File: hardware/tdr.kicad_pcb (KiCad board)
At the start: 4 copper layers, 232 parts, among them J201 Conn_02x01, J202 Conn_Coaxial, J203 Conn_Coaxial, J204 Conn_Coaxial, J205 Conn_Coaxial, J206 Conn_Coaxial, J207 Conn_Coaxial, J208 Conn_Coaxial, J209 Conn_Coaxial, J210 Barrel_Jack_Switch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

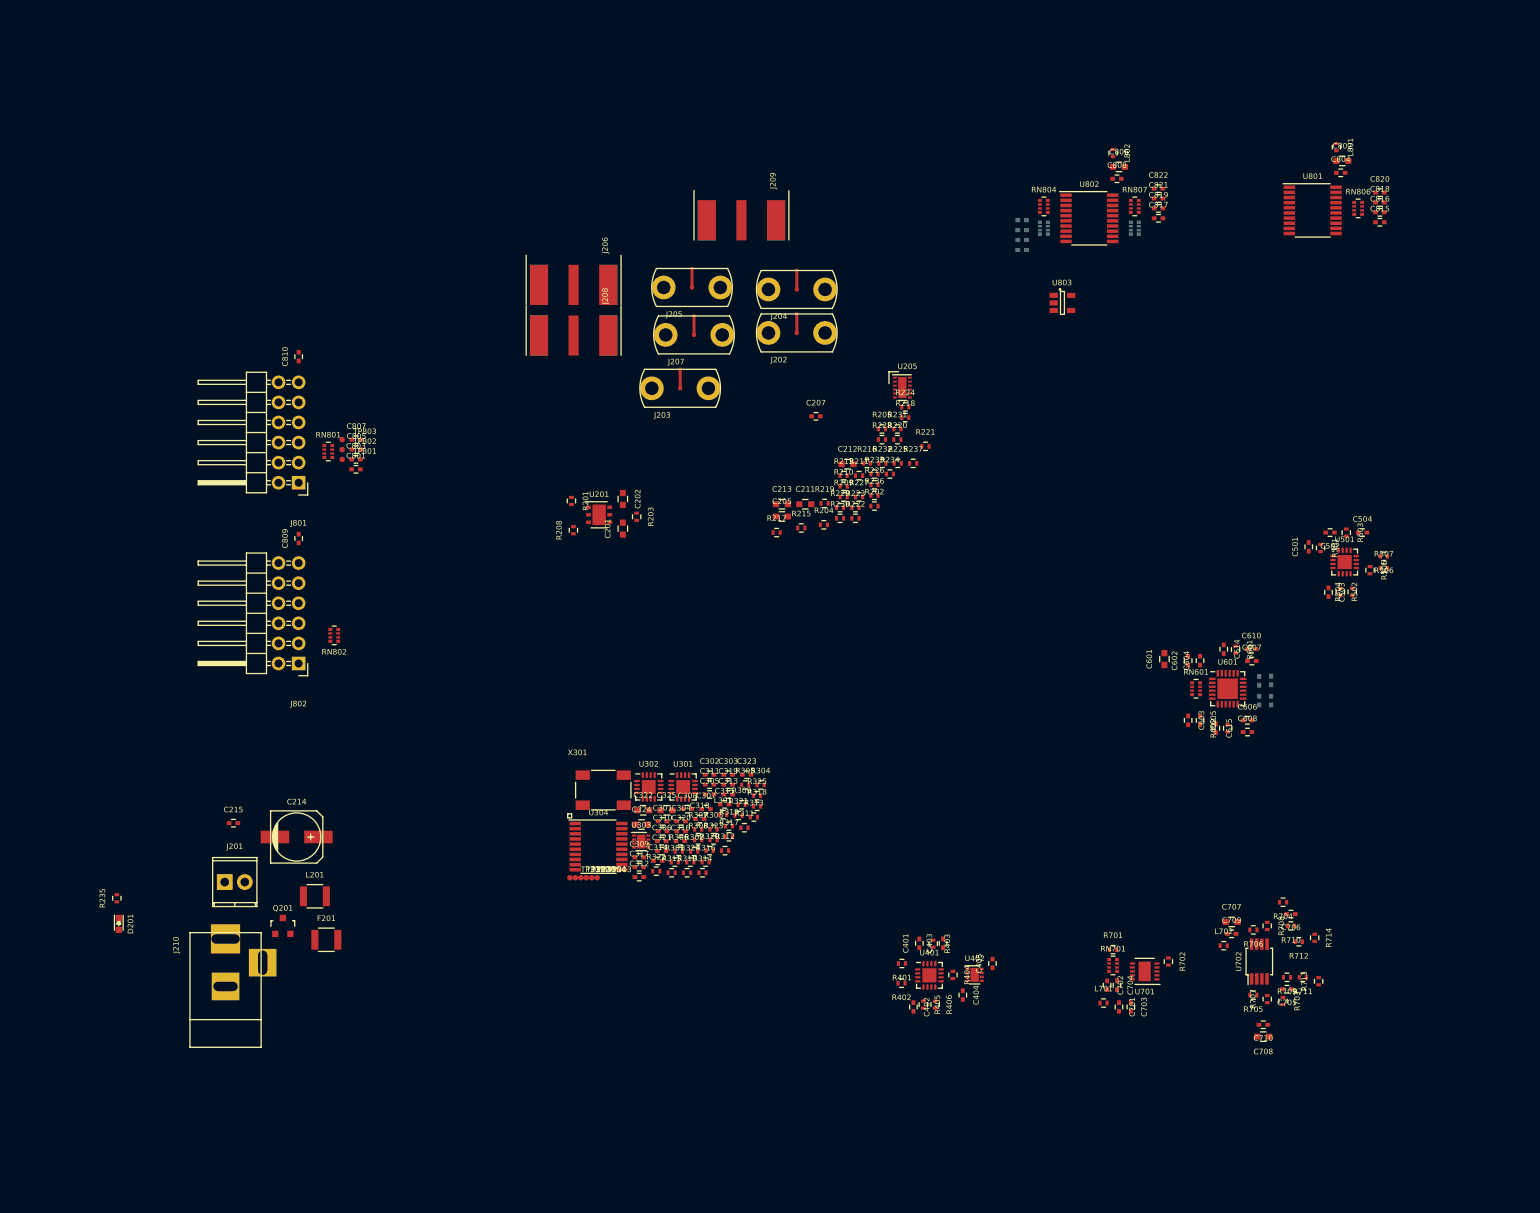
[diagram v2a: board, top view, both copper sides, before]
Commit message: more component placement on tdr..
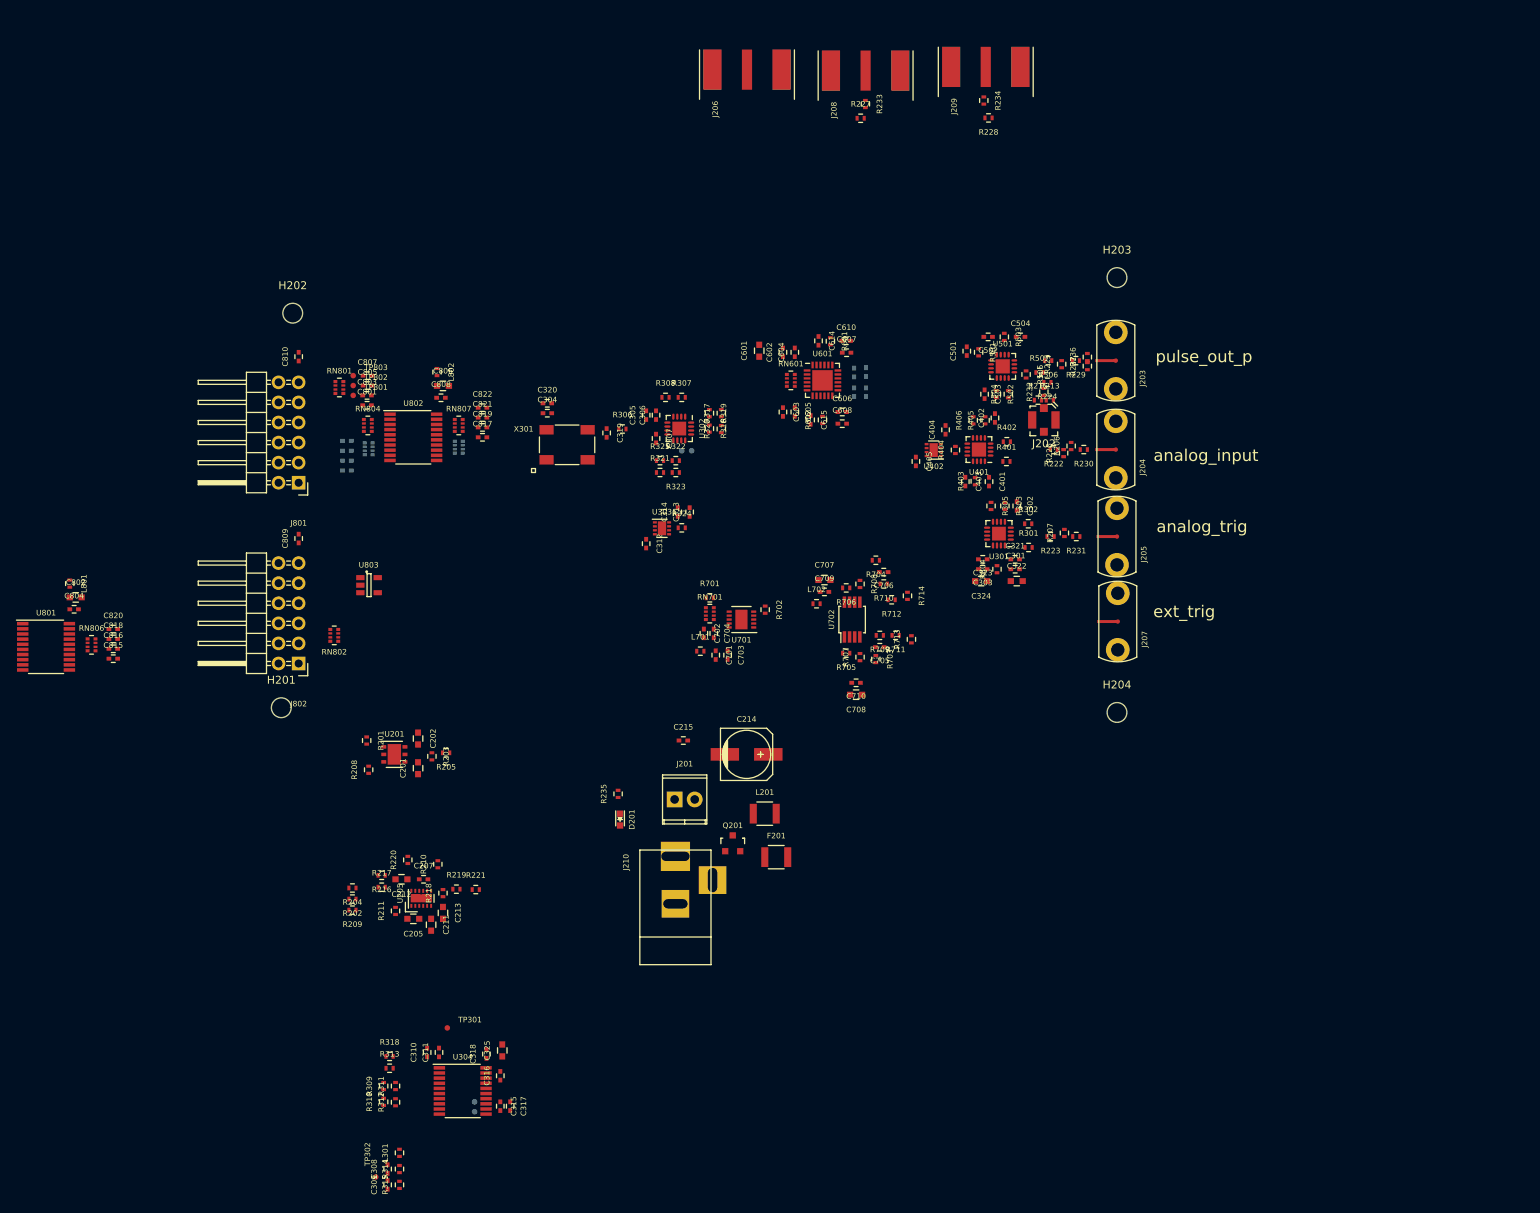
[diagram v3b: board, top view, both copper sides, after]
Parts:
- added H201: MountingHole, Mounting_Holes:MountingHole_2-5mm, F.Cu at (92.8, 104.4)
- added H202: MountingHole, Mounting_Holes:MountingHole_2-5mm, F.Cu at (94.2, 54.5)
- added H203: MountingHole, Mounting_Holes:MountingHole_2-5mm, F.Cu at (198.5, 50.0)
- added H204: MountingHole, Mounting_Holes:MountingHole_2-5mm, F.Cu at (198.5, 105.0)
- added R206: DNP, Resistors_SMD:R_0402, F.Cu at (192.7, 71.3)
- added R207: DNP, Resistors_SMD:R_0402, F.Cu at (191.8, 82.3)
- J202: footprint vna_footprints:SF2921-61345 -> vna_footprints:734120110_ufl_umc
- TP303, TP304, TP305, TP306: moved to B.Cu
- moved C804 169.4 mm to (66.6, 92.0)
- moved C802 169.4 mm to (66.8, 90.5)
- moved C815 169.4 mm to (71.5, 98.2)
- moved C816 169.4 mm to (71.5, 97.0)
- moved C818 169.4 mm to (71.5, 95.7)
- moved C820 169.4 mm to (71.5, 94.5)
- moved L801 169.4 mm to (66.0, 88.7)
- moved RN806 169.4 mm to (68.8, 96.5)
- moved U801 169.4 mm to (63.0, 96.7)
- moved U803 94.7 mm to (103.9, 88.9)
- moved C806 89.9 mm to (113.2, 63.7)
- moved C808 89.9 mm to (113.0, 65.2)
- moved C817 89.9 mm to (118.2, 70.2)
- moved C819 89.9 mm to (118.2, 69.0)
- moved C821 89.9 mm to (118.2, 67.7)
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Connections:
- R222 pad 1: Net-(R222-Pad1) -> Net-(R206-Pad1)
- R223 pad 1: Net-(R223-Pad1) -> Net-(R207-Pad1)
- R225 pad 1: Net-(R222-Pad1) -> Net-(R206-Pad2)
- R226 pad 1: Net-(R223-Pad1) -> Net-(R207-Pad2)
- R226 pad 2: Net-(R222-Pad1) -> Net-(R206-Pad1)
- R230 pad 2: Net-(R222-Pad1) -> Net-(R206-Pad1)
- R231 pad 2: Net-(R223-Pad1) -> Net-(R207-Pad1)
- R236 pad 2: (no net) -> GND
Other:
- board text added: "analog_input"
- board text added: "analog_trig"
- board text added: "ext_trig"
- board text added: "pulse_out_p"

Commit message: added rf crossover for latch trigger line to help with layout
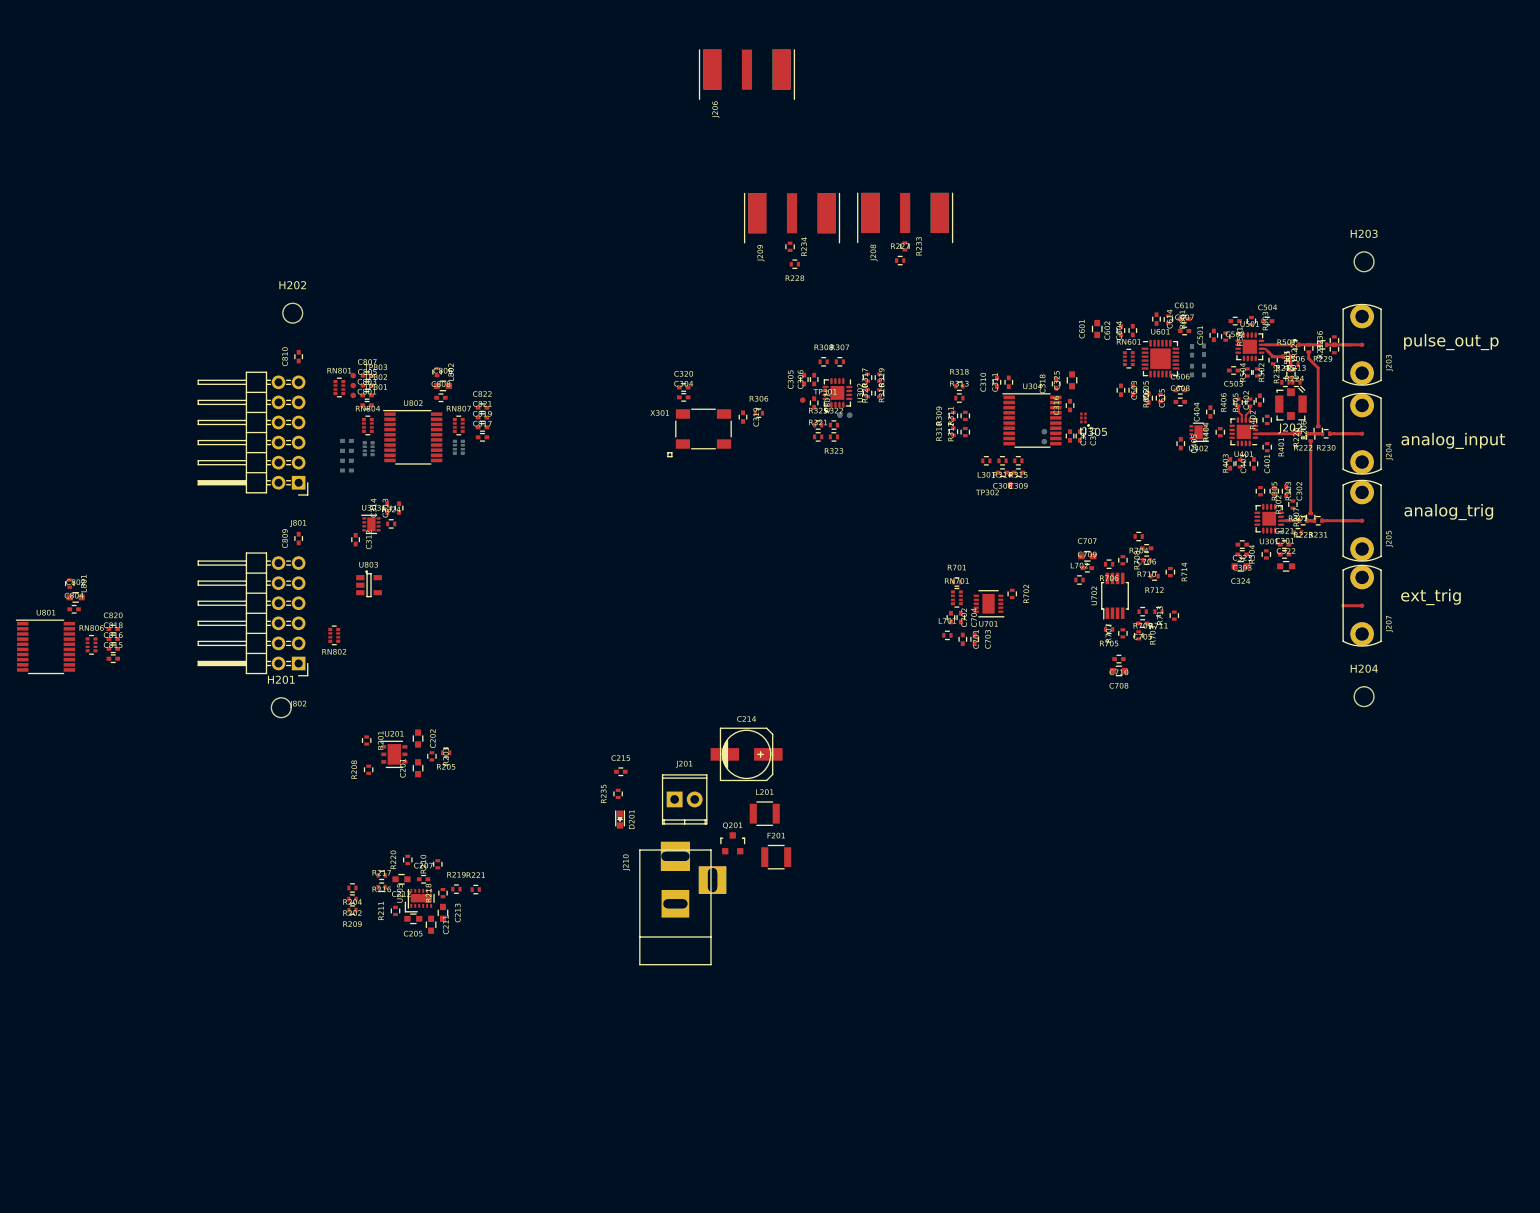
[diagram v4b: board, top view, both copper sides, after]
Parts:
- added U305: X0060L5050AHF, synth_footprints:X0060L5050AHF, F.Cu at (194.2, 67.8)
- moved R315 120.5 mm to (186.0, 73.2), turned to 180 degrees
- moved C309 120.3 mm to (186.0, 74.7), turned to 180 degrees
- moved TP302 118.8 mm to (185.0, 76.2), turned to 180 degrees
- moved R314 117.7 mm to (184.0, 73.2), turned to 180 degrees
- moved C308 117.5 mm to (184.0, 74.7), turned to 180 degrees
- moved L301 114.8 mm to (182.0, 73.2), turned to 180 degrees
- moved U304 111.3 mm to (187.8, 68.1)
- moved C310 111.3 mm to (183.3, 63.2)
- moved C311 111.3 mm to (184.8, 63.2)
- moved C315 111.3 mm to (192.6, 70.0)
- moved C317 111.3 mm to (193.8, 70.0)
- moved C325 111.3 mm to (192.8, 63.0)
- moved R309 111.3 mm to (177.8, 67.5)
- moved R310 111.3 mm to (177.8, 69.5)
- moved R311 111.3 mm to (179.3, 67.5)
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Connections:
- R405 pad 2: /delay_pulse/~DELAY1_OUT -> /~LATCH
- R406 pad 2: /delay_pulse/DELAY1_OUT -> /LATCH
- U304 pad 15: /CLK_SAMPLE_N -> Net-(U304-Pad15)
- U304 pad 16: /CLK_SAMPLE_P -> Net-(U304-Pad16)
- U601 pad 13: /delay_pulse/~DELAY1_OUT -> /LATCH
- U601 pad 14: /delay_pulse/DELAY1_OUT -> /~LATCH
- U601 pad 8: /CLK_SAMPLE_P -> /CLK_SAMPLE_N
- U601 pad 9: /CLK_SAMPLE_N -> /CLK_SAMPLE_P
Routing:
- net Net-(R206-Pad2): track 0.00 -> 9.95 mm
- net Net-(R207-Pad2): track 0.00 -> 9.20 mm
- net /conn_power/ANALOG_INPUT: track 0.00 -> 5.59 mm
- net Net-(J205-Pad1): track 0.00 -> 4.05 mm
- net Net-(R506-Pad2): track 0.00 -> 3.83 mm
- net Net-(J203-Pad1): track 0.00 -> 3.30 mm
- net Net-(R505-Pad1): track 0.00 -> 3.14 mm
- net Net-(J204-Pad1): track 0.00 -> 2.90 mm
- net /conn_power/PULSE_OUT_P: track 0.00 -> 2.60 mm
- net /EXT_ANALOG_TRIG: track 0.00 -> 2.59 mm
- net Net-(R206-Pad1): track 0.00 -> 2.00 mm
- net Net-(R405-Pad1): track 0.00 -> 1.99 mm
- net Net-(R406-Pad1): track 0.00 -> 1.97 mm
- net /conn_power/PULSE_OUT_N: track 0.00 -> 1.04 mm
- net Net-(R207-Pad1): track 0.00 -> 1.00 mm

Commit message: more component placement on tdr..
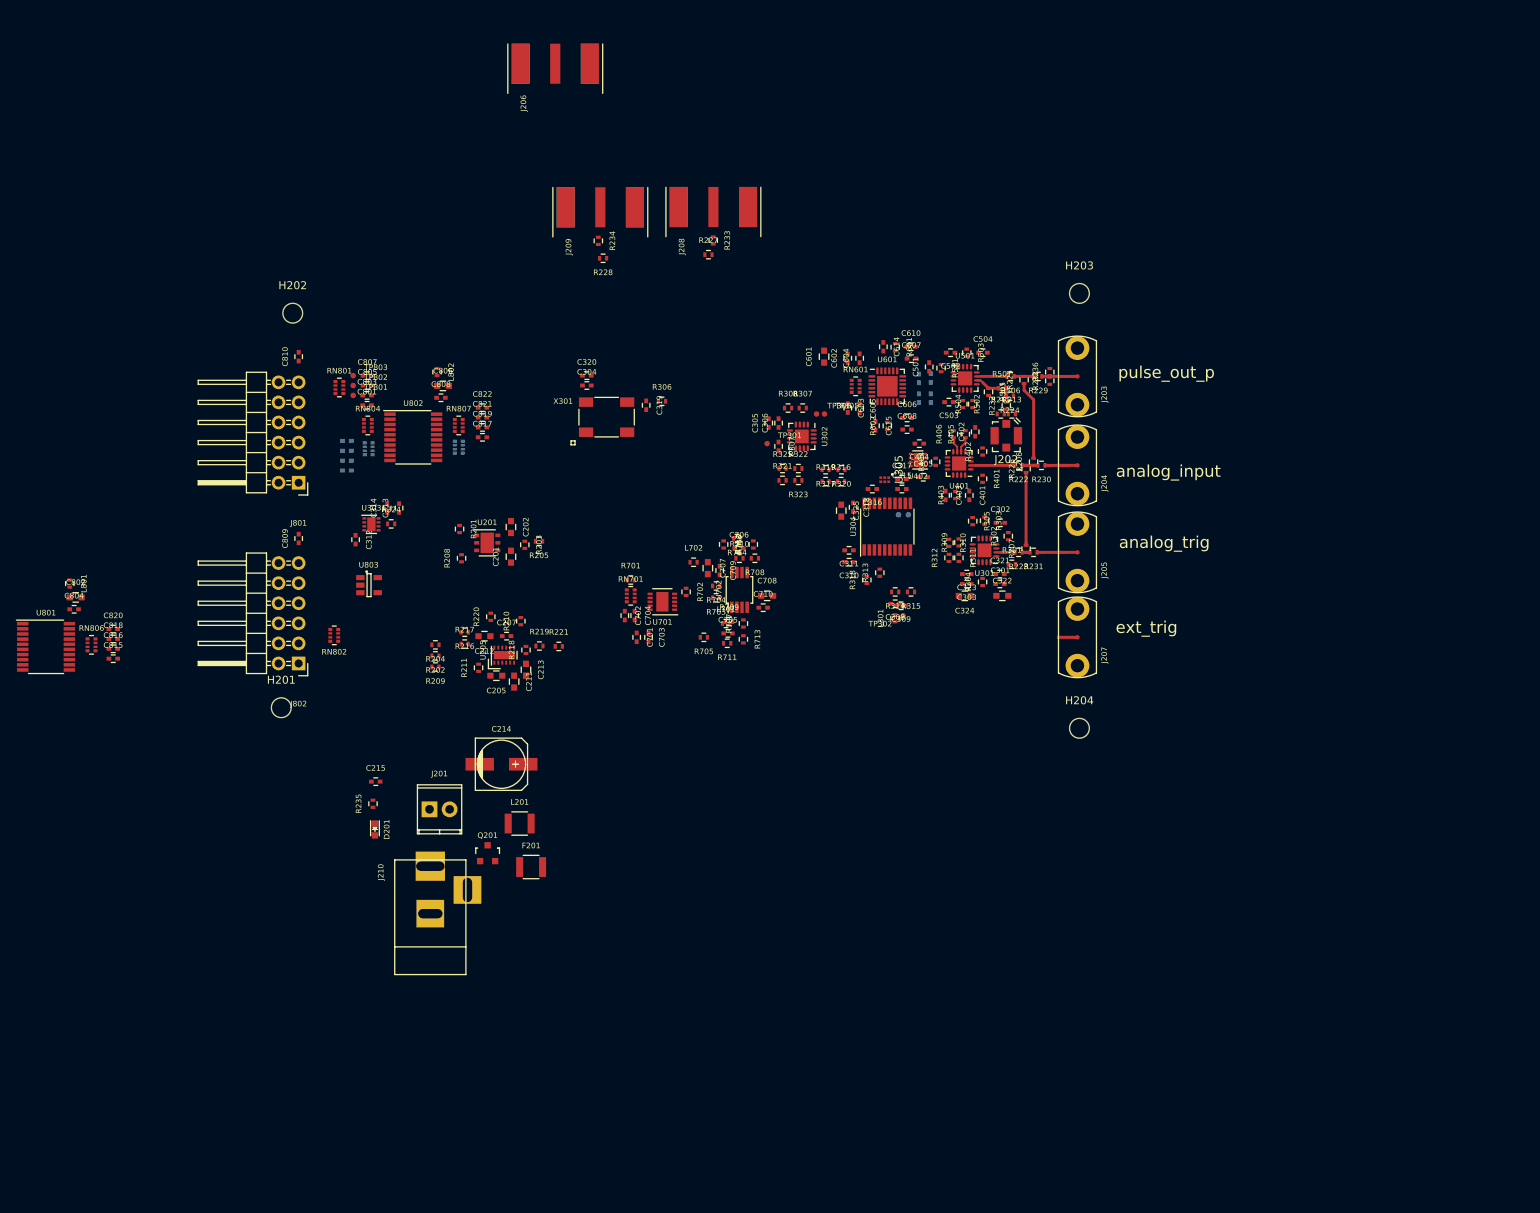
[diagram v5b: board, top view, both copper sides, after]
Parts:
- C302, C405: value .01 uF -> 10 nF
- TP305, TP306: moved to F.Cu
- moved R714 55.0 mm to (150.4, 83.0), turned to 180 degrees
- moved R711 54.7 mm to (149.2, 96.2)
- moved R712 54.6 mm to (148.8, 83.8), turned to 270 degrees
- moved R713 54.6 mm to (151.2, 95.8), turned to 270 degrees
- moved R704 53.8 mm to (147.8, 89.0)
- moved R703 53.7 mm to (147.8, 90.5), turned to 180 degrees
- moved C705 52.5 mm to (149.3, 95.0), turned to 0 degrees
- moved R709 52.3 mm to (149.4, 93.5), turned to 0 degrees
- moved C706 51.6 mm to (150.7, 84.2), turned to 0 degrees
- moved R710 51.5 mm to (150.8, 85.5), turned to 0 degrees
- moved R705 51.3 mm to (146.2, 95.5)
- moved L702 48.9 mm to (144.9, 86.0)
- moved C707 48.0 mm to (146.8, 86.8), turned to 270 degrees
- moved R707 48.0 mm to (151.2, 93.8)
- moved U702 47.5 mm to (150.8, 89.5)
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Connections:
- U302 pad 11: Net-(TP305-Pad1) -> Net-(R316-Pad1)
- U302 pad 12: Net-(TP306-Pad1) -> Net-(R317-Pad1)
- U302 pad 15: Net-(R316-Pad1) -> Net-(TP305-Pad1)
- U302 pad 16: Net-(R317-Pad1) -> Net-(TP306-Pad1)
- U304 pad 6: Net-(R311-Pad1) -> /EXT_TRIG
- U304 pad 7: Net-(R309-Pad1) -> Net-(C309-Pad1)
- U304 pad 8: /EXT_TRIG -> Net-(R311-Pad1)
- U304 pad 9: Net-(C309-Pad1) -> Net-(R309-Pad1)
